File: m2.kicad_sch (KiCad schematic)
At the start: 4 parts, among them J2 Bus_M.2_Socket_M, Y1 SG-3030CM

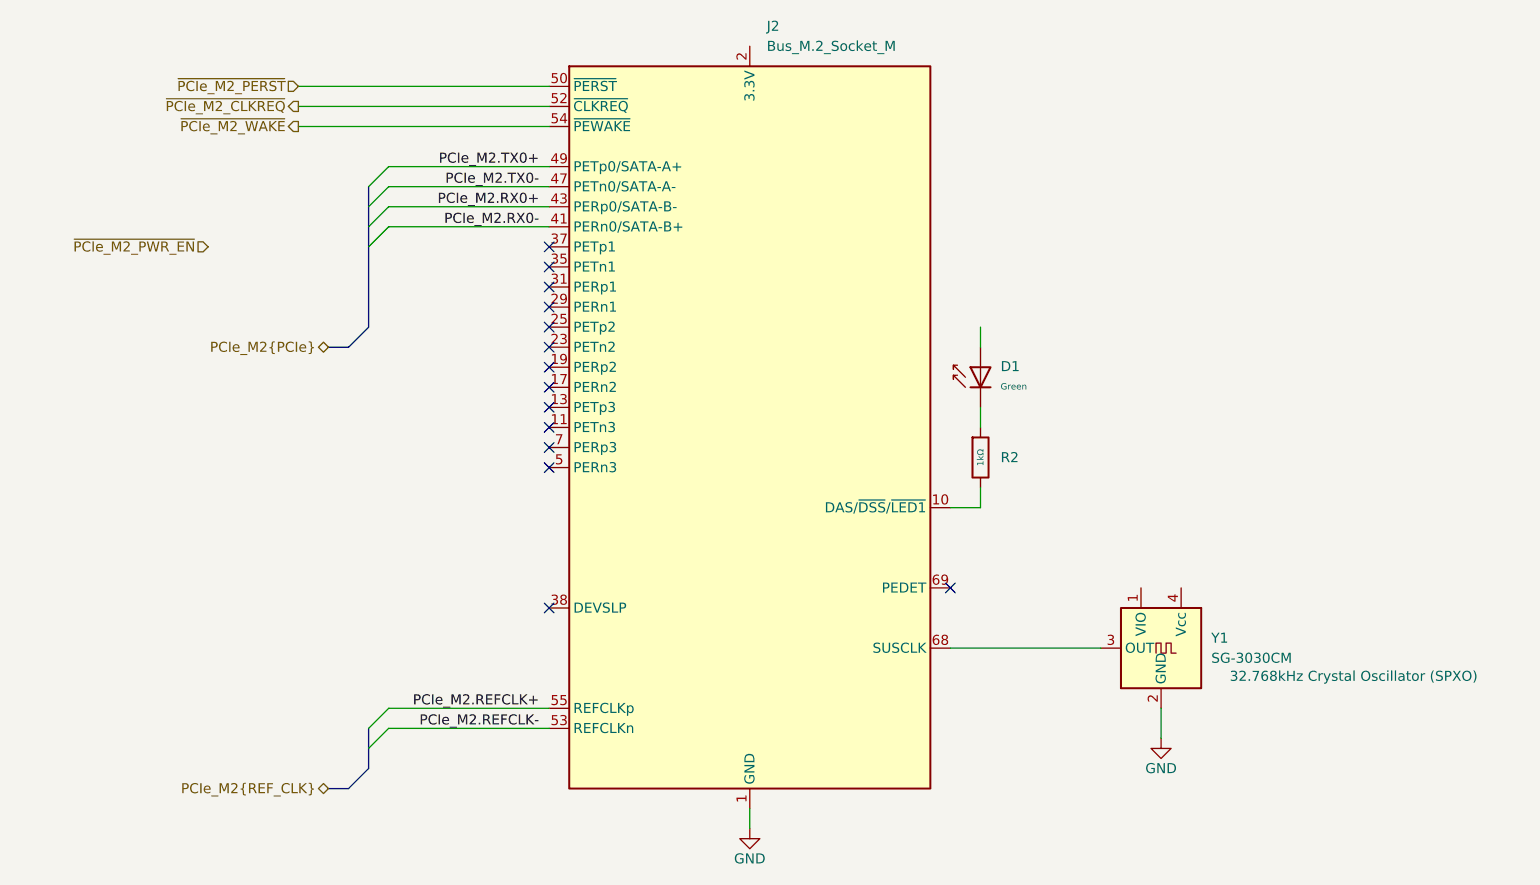
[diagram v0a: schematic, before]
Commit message: [#1] WIP: Change components to ones from the global library, refactor schematic
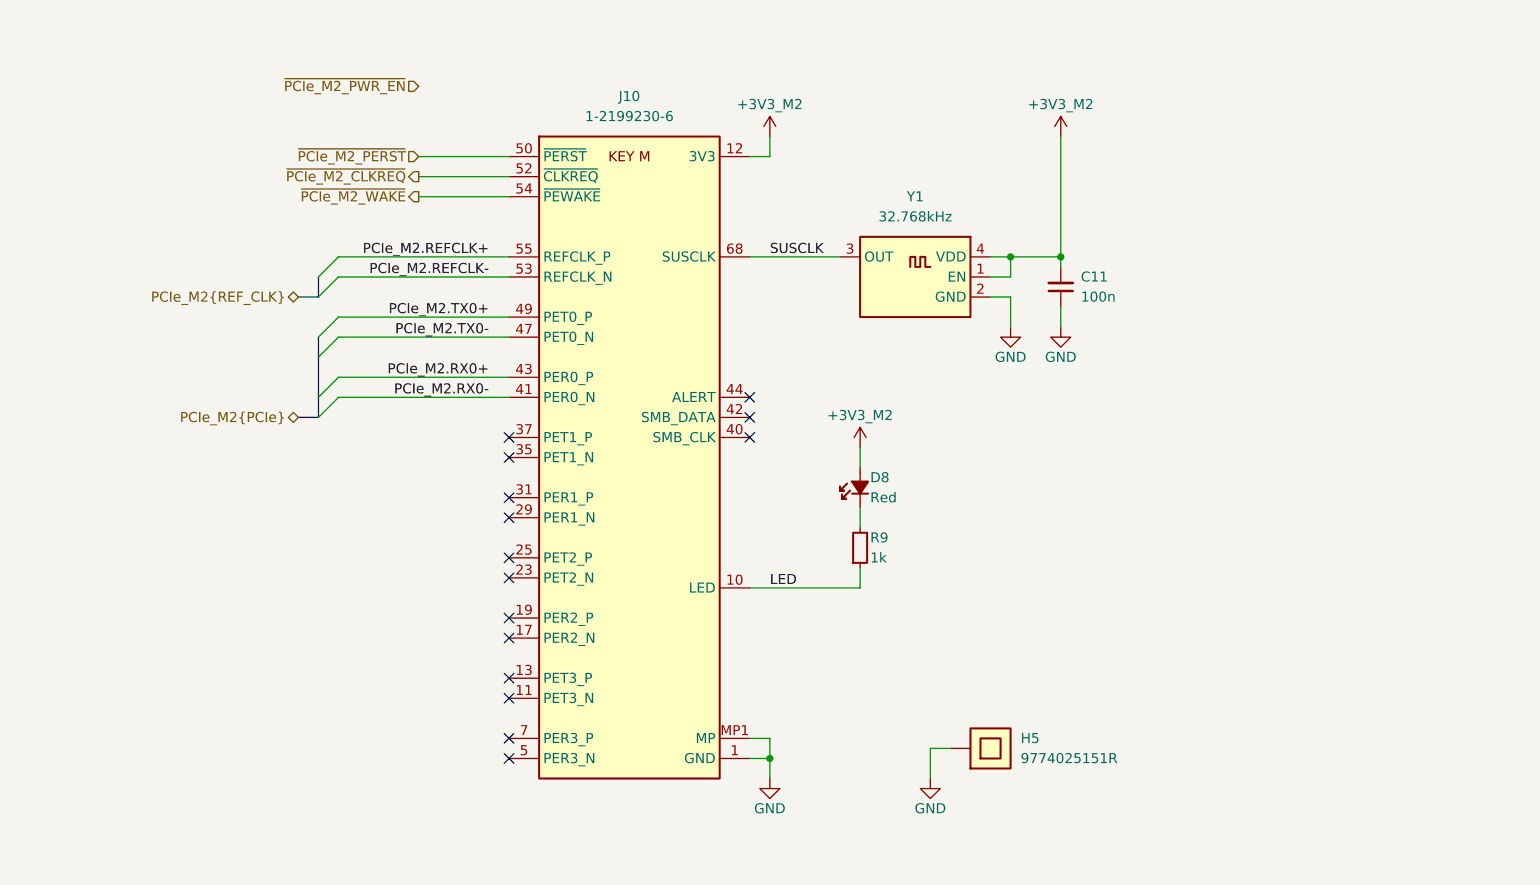
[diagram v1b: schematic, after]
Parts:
- removed D1: Green, PCM_JLCPCB:D_0603, symbol PCM_JLCPCB-Diodes:LED,0603,Green
- removed J2: Bus_M.2_Socket_M, lib:M.2 M Key socket, symbol Connector:Bus_M.2_Socket_M
- removed R2: 1kΩ, PCM_JLCPCB:R_0402, symbol PCM_JLCPCB-Resistors:0402,1kΩ
- removed Y1: SG-3030CM, Oscillator:Oscillator_SMD_SeikoEpson_SG3030CM, symbol Oscillator:SG-3030CM
- added C11: C-100n-0402, DW-footprints:C_0402_1005Metric, symbol DW-capacitors:C-100n-0402
- added D8: LED-R-0603_KT-0603R, DW-footprints:LED_0603_1608Metric_R, symbol DW-diodes:LED-R-0603_KT-0603R
- added H5: Spacer_M2.5_H2.5mm_9774025151R, DW-footprints:Spacer_M2.5_H2.5mm_9774025151R, symbol DW-mechanical:Spacer_M2.5_H2.5mm_9774025151R
- added J10: Bus_M.2_1-2199230-6, DW-footprints:Bus_M.2_Socket_Key_M_TE_1-2199230-6, symbol DW-connectors:Bus_M.2_1-2199230-6
- added R9: R-1k-0402, DW-footprints:R_0402_1005Metric, symbol DW-resistors:R-1k-0402
- added Y1: Oscillator_32.768kHz_OK2EL89CJI-111YLC-32.768K, DW-footprints:Crystal_SMD_3225-4Pin_3.2x2.5mm, symbol DW-crystals:Oscillator_32.768kHz_OK2EL89CJI-111YLC-32.768K
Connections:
- net GND: now also C11.1, H5.1, J10.1 (GND), J10.15 (GND), J10.21 (GND), J10.27 (GND), J10.3 (GND), J10.33 (GND), J10.39 (GND), J10.45 (GND), J10.51 (GND), J10.57 (GND), J10.71 (GND), J10.73 (GND), J10.75 (GND), J10.9 (GND), J10.MP1 (MP), J10.MP2 (MP), Y1.2 (GND)
- net PCIe_M2.REFCLK+: now also J10.55 (REFCLK_P)
- net PCIe_M2.REFCLK-: now also J10.53 (REFCLK_N)
- net PCIe_M2.RX0+: now also J10.43 (PER0_P)
- net PCIe_M2.RX0-: now also J10.41 (PER0_N)
- net PCIe_M2.TX0+: now also J10.49 (PET0_P)
- net PCIe_M2.TX0-: now also J10.47 (PET0_N)
- net ~{PCIe_M2_CLKREQ}: now also J10.52 (~{CLKREQ})
- net ~{PCIe_M2_PERST}: now also J10.50 (~{PERST})
- net ~{PCIe_M2_WAKE}: now also J10.54 (~{PEWAKE})
- new net: D8.1 (C), R9.2
- new net: J10.20 (NC), J10.22 (NC), J10.24 (NC), J10.26 (NC), J10.28 (NC), J10.30 (NC), J10.32 (NC), J10.34 (NC), J10.36 (NC), J10.38 (NC), J10.46 (NC), J10.48 (NC), J10.56 (NC), J10.58 (NC), J10.6 (NC), J10.67 (NC), J10.69 (NC), J10.8 (NC)
- new net +3V3_M2: C11.2, D8.2 (A), J10.12 (3V3), J10.14 (3V3), J10.16 (3V3), J10.18 (3V3), J10.2 (3V3), J10.4 (3V3), J10.70 (3V3), J10.72 (3V3), J10.74 (3V3), Y1.1 (EN), Y1.4 (VDD)
- new net LED: J10.10 (LED), R9.1
- new net SUSCLK: J10.68 (SUSCLK), Y1.3 (OUT)
- no-connect marks 14 -> 15

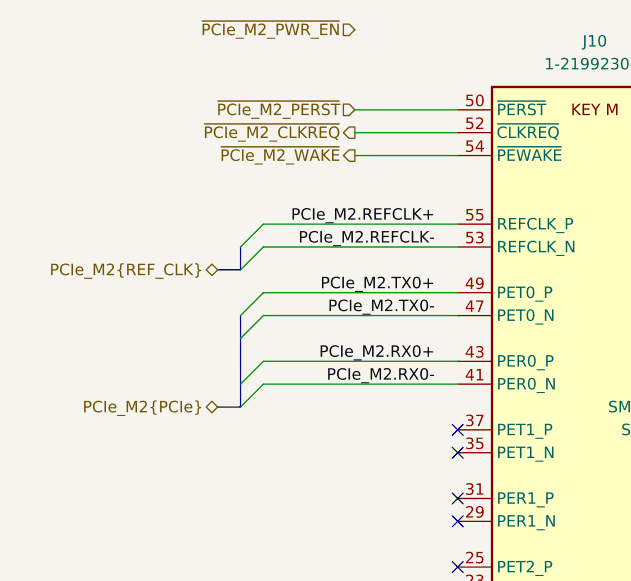
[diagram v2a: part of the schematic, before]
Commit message: [#1] Add bus colors, rename PCIe signals
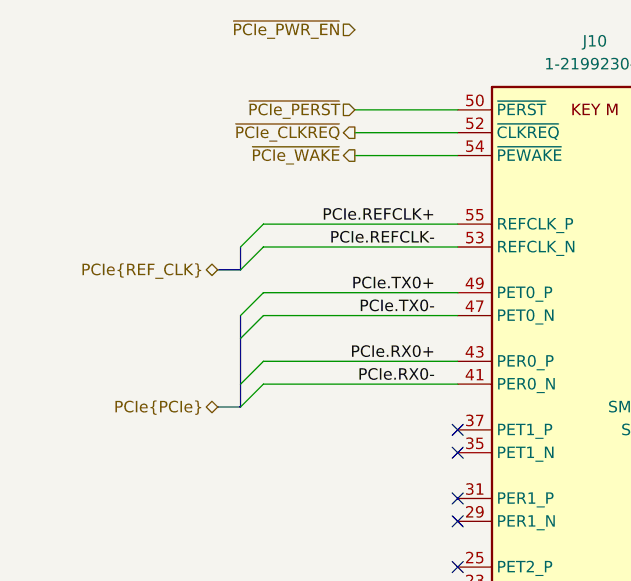
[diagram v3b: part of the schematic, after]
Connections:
- net PCIe_M2.REFCLK+ renamed PCIe.REFCLK+
- net PCIe_M2.REFCLK- renamed PCIe.REFCLK-
- net PCIe_M2.RX0+ renamed PCIe.RX0+
- net PCIe_M2.RX0- renamed PCIe.RX0-
- net PCIe_M2.TX0+ renamed PCIe.TX0+
- net PCIe_M2.TX0- renamed PCIe.TX0-
- net ~{PCIe_M2_CLKREQ} renamed ~{PCIe_CLKREQ}
- net ~{PCIe_M2_PERST} renamed ~{PCIe_PERST}
- net ~{PCIe_M2_WAKE} renamed ~{PCIe_WAKE}

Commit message: [#1] Re-annotate schematic
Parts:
- renumbered C11 to C1, D8 to D2, J10 to J5, R9 to R7
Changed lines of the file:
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@@
 		(on_board yes)
 		(dnp no)
-		(property "Reference" "#PWR044"
+		(property "Reference" "#PWR022"
 			(at 213.36 105.41 0)
 			(effects
@@
 			(project ""
 				(path "/090a8e41-87a8-4fb1-998b-60a2c0dc4cee/18a4552b-ac02-46c8-954e-f58b32a322f0"
-					(reference "#PWR044")
+					(reference "#PWR022")
 					(unit 1)
 				)
@@
 		(on_board yes)
 		(dnp no)
-		(property "Reference" "#PWR17"
+		(property "Reference" "#PWR024"
 			(at 243.84 132.08 0)
 			(effects
@@
 			(project "cm5-module"
 				(path "/090a8e41-87a8-4fb1-998b-60a2c0dc4cee/18a4552b-ac02-46c8-954e-f58b32a322f0"
-					(reference "#PWR17")
+					(reference "#PWR024")
 					(unit 1)
 				)
@@
 		(on_board yes)
 		(dnp no)
-		(property "Reference" "R9"
+		(property "Reference" "R7"
 			(at 226.06 152.4 90)
 			(effects
@@
 			(project ""
 				(path "/090a8e41-87a8-4fb1-998b-60a2c0dc4cee/18a4552b-ac02-46c8-954e-f58b32a322f0"
-					(reference "R9")
+					(reference "R7")
 					(unit 1)
 				)
@@
 		(dnp no)
 		(fields_autoplaced yes)
-		(property "Reference" "C11"
+		(property "Reference" "C1"
 			(at 252.73 119.3736 90)
 			(effects
@@
 			(project ""
 				(path "/090a8e41-87a8-4fb1-998b-60a2c0dc4cee/18a4552b-ac02-46c8-954e-f58b32a322f0"
-					(reference "C11")
+					(reference "C1")
 					(unit 1)
 				)
@@
 		(dnp no)
 		(fields_autoplaced yes)
-		(property "Reference" "J10"
+		(property "Reference" "J5"
 			(at 195.58 96.52 0)
 			(effects
@@
 			(project ""
 				(path "/090a8e41-87a8-4fb1-998b-60a2c0dc4cee/18a4552b-ac02-46c8-954e-f58b32a322f0"
-					(reference "J10")
+					(reference "J5")
 					(unit 1)
 				)
@@
 		(on_board yes)
 		(dnp no)
-		(property "Reference" "#PWR019"
+		(property "Reference" "#PWR025"
 			(at 250.19 132.08 0)
 			(effects
@@
 			(project "cm5-module"
 				(path "/090a8e41-87a8-4fb1-998b-60a2c0dc4cee/18a4552b-ac02-46c8-954e-f58b32a322f0"
-					(reference "#PWR019")
+					(reference "#PWR025")
 					(unit 1)
 				)
@@
 		(on_board yes)
 		(dnp no)
-		(property "Reference" "#PWR18"
+		(property "Reference" "#PWR027"
 			(at 213.36 189.23 0)
 			(effects
@@
 			(project "cm5-module"
 				(path "/090a8e41-87a8-4fb1-998b-60a2c0dc4cee/18a4552b-ac02-46c8-954e-f58b32a322f0"
-					(reference "#PWR18")
+					(reference "#PWR027")
 					(unit 1)
 				)
@@
 		(on_board yes)
 		(dnp no)
-		(property "Reference" "#PWR046"
+		(property "Reference" "#PWR026"
 			(at 224.79 144.78 0)
 			(effects
@@
 			(project "cm5-module"
 				(path "/090a8e41-87a8-4fb1-998b-60a2c0dc4cee/18a4552b-ac02-46c8-954e-f58b32a322f0"
-					(reference "#PWR046")
+					(reference "#PWR026")
 					(unit 1)
 				)
@@
 		(on_board yes)
 		(dnp no)
-		(property "Reference" "#PWR045"
+		(property "Reference" "#PWR023"
 			(at 250.19 105.41 0)
 			(effects
@@
 			(project "cm5-module"
 				(path "/090a8e41-87a8-4fb1-998b-60a2c0dc4cee/18a4552b-ac02-46c8-954e-f58b32a322f0"
-					(reference "#PWR045")
+					(reference "#PWR023")
 					(unit 1)
 				)
@@
 		(on_board yes)
 		(dnp no)
-		(property "Reference" "#PWR022"
+		(property "Reference" "#PWR028"
 			(at 233.68 189.23 0)
 			(effects
@@
 			(project "cm5-module"
 				(path "/090a8e41-87a8-4fb1-998b-60a2c0dc4cee/18a4552b-ac02-46c8-954e-f58b32a322f0"
-					(reference "#PWR022")
+					(reference "#PWR028")
 					(unit 1)
 				)
@@
 		(on_board yes)
 		(dnp no)
-		(property "Reference" "D8"
+		(property "Reference" "D2"
 			(at 226.06 144.78 90)
 			(effects
@@
 			(project "cm5-module"
 				(path "/090a8e41-87a8-4fb1-998b-60a2c0dc4cee/18a4552b-ac02-46c8-954e-f58b32a322f0"
-					(reference "D8")
+					(reference "D2")
 					(unit 1)
 				)

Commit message: [#1] Sync PCB with schematic, draft component placement
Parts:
- added A2: M.2 M-key 2280, DW-footprints:Card_M.2-2280-M-key, symbol DW-mechanical:Card_M.2-2280-M-key
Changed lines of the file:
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@@
+	)
+	(symbol
+		(lib_id "DW-mechanical:Card_M.2-2280-M-key")
+		(at 281.94 134.62 0)
+		(unit 1)
+		(exclude_from_sim no)
+		(in_bom no)
+		(on_board yes)
+		(dnp no)
+		(fields_autoplaced yes)
+		(property "Reference" "A2"
+			(at 313.69 128.27 0)
+			(effects
+				(font
+					(size 1.27 1.27)
+					(thickness 0.15)
+				)
+			)
+		)
+		(property "Value" "M.2 M-key 2280"
+			(at 313.69 130.81 0)
+			(effects
+				(font
+					(size 1.27 1.27)
+					(thickness 0.15)
+				)
+			)
+		)
+		(property "Footprint" "DW-footprints:Card_M.2-2280-M-key"
+			(at 346.71 139.7 0)
+			(effects
+				(font
+					(size 1.27 1.27)
+					(thickness 0.15)
+				)
+				(justify left bottom)
+				(hide yes)
+			)
+		)
+		(property "Datasheet" ""
+			(at 346.71 142.24 0)
+			(effects
+				(font
+					(size 1.27 1.27)
+					(thickness 0.15)
+				)
+				(justify left bottom)
+				(hide yes)
+			)
+		)
+		(property "Description" "M.2, Key M, 2280, generic NVMe, SSD"
+			(at 346.71 144.78 0)
+			(effects
+				(font
+					(size 1.27 1.27)
+					(thickness 0.15)
+				)
+				(justify left bottom)
+				(hide yes)
+			)
+		)
+		(instances
+			(project ""
+				(path "/090a8e41-87a8-4fb1-998b-60a2c0dc4cee/18a4552b-ac02-46c8-954e-f58b32a322f0"
+					(reference "A2")
+					(unit 1)
+				)
+			)
+		)
 	)
 	(symbol

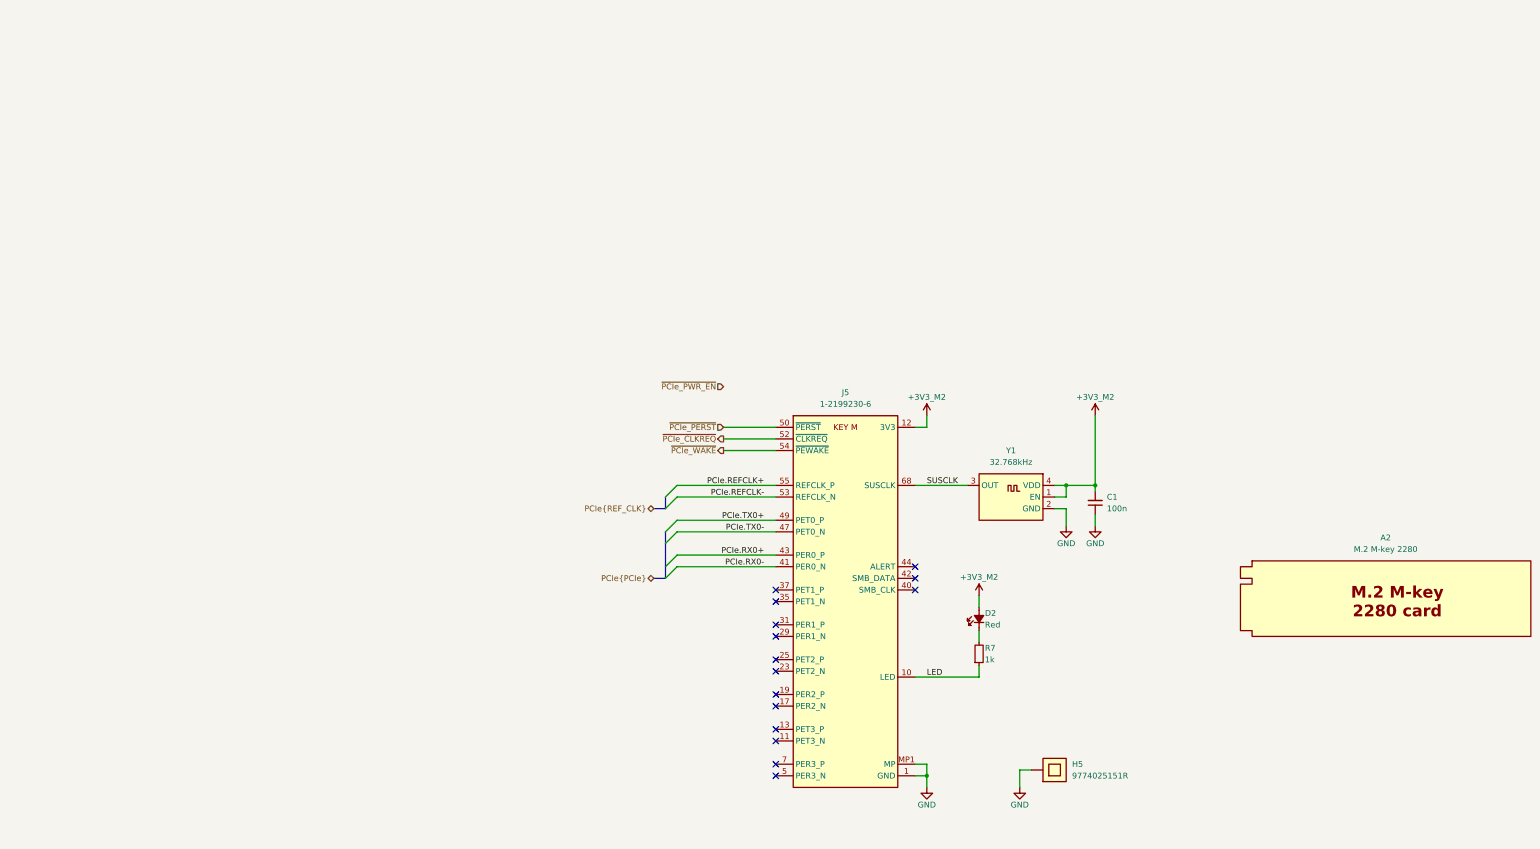
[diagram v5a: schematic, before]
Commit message: [#1] WIP: Refactor schematic
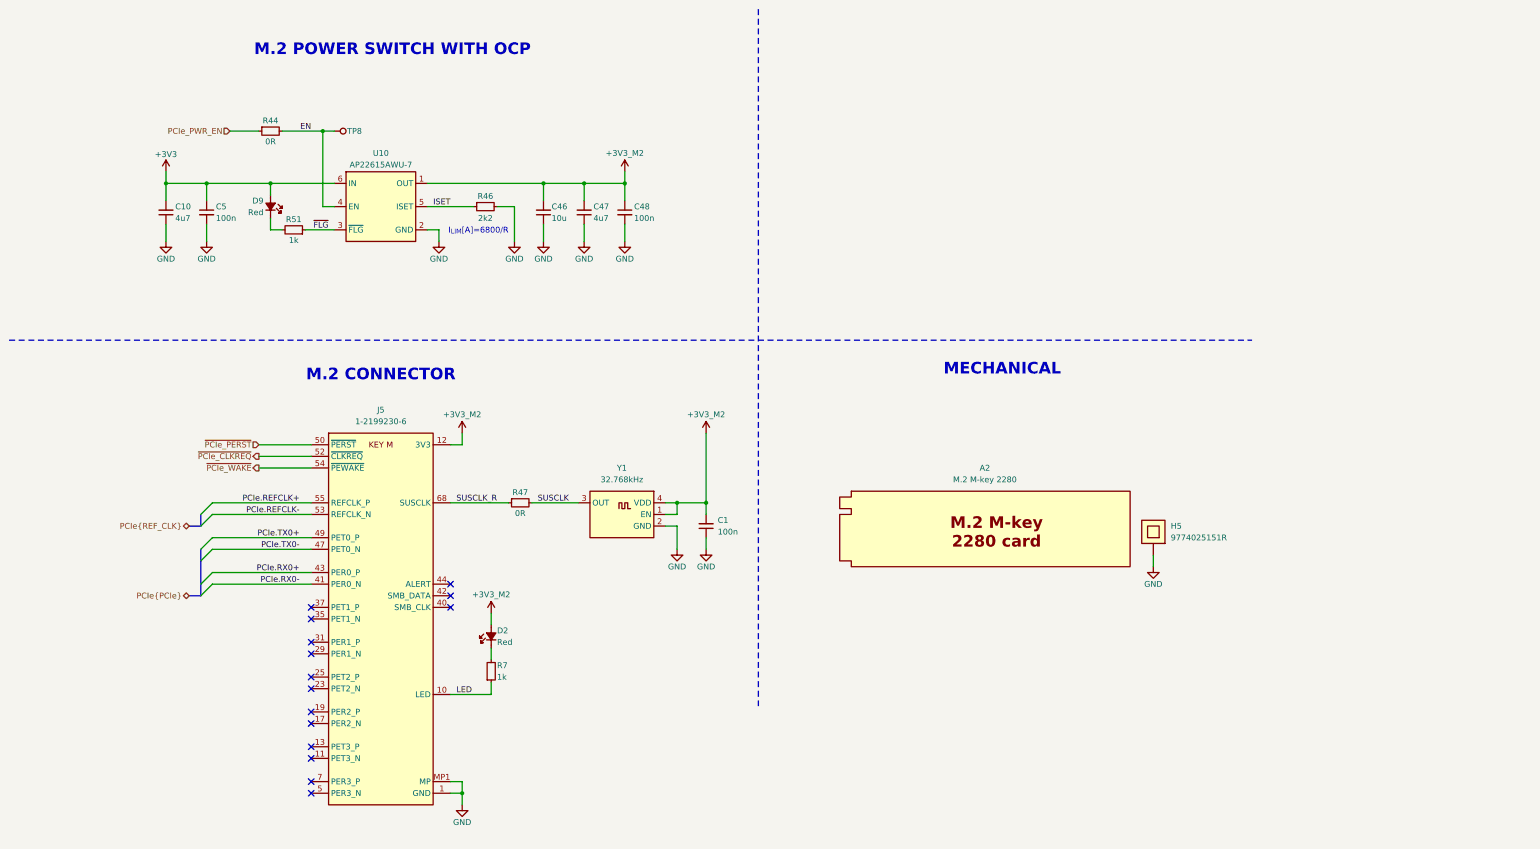
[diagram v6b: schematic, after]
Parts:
- added C10, C47: C-4u7-0402, DW-footprints:C_0402_1005Metric, symbol DW-capacitors:C-4u7-0402
- added C46: C-10u-0603, DW-footprints:C_0603_1608Metric, symbol DW-capacitors:C-10u-0603
- added C48, C5: C-100n-0402, DW-footprints:C_0402_1005Metric, symbol DW-capacitors:C-100n-0402
- added D9: LED-R-0603_KT-0603R, DW-footprints:LED_0603_1608Metric_R, symbol DW-diodes:LED-R-0603_KT-0603R
- added R44, R47: R-0R-0402, DW-footprints:R_0402_1005Metric, symbol DW-resistors:R-0R-0402
- added R46: R-2k2-0402, DW-footprints:R_0402_1005Metric, symbol DW-resistors:R-2k2-0402
- added R51: R-1k-0402, DW-footprints:R_0402_1005Metric, symbol DW-resistors:R-1k-0402
- added TP8: TP_SMD_0.75mm, DW-footprints:TP_SMD_0.75mm, symbol DW-test-points:TP_SMD_0.75mm
- added U10: AP22615AWU-7, DW-footprints:TSOT-23-6, symbol DW-ICs:AP22615AWU-7
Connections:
- net +3V3_M2: now also C46.2, C47.2, C48.1, U10.1 (OUT)
- net GND: now also C10.1, C46.1, C47.1, C48.2, C5.2, R46.2, U10.2 (GND)
- net SUSCLK: now also R47.2; no longer J5.68 (SUSCLK)
- new net: D9.1 (C), R51.2
- new net +3V3: C10.2, C5.1, D9.2 (A), U10.6 (IN)
- new net EN: R44.2, TP8.1, U10.4 (EN)
- new net ISET: R46.1, U10.5 (ISET)
- new net PCIe_PWR_EN: R44.1
- new net SUSCLK_R: J5.68 (SUSCLK), R47.1
- new net ~{FLG}: R51.1, U10.3 (~{FLG})
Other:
- note added: "I_{LIM}[A]=6800/R"
- note added: "M.2 CONNECTOR"
- note added: "M.2 POWER SWITCH WITH OCP"
- note added: "MECHANICAL"
- moved on the sheet: A2, C1, D2, H5, J5, R7, Y1
